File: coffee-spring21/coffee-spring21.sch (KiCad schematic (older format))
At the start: 54 parts, among them J1 AudioPlug3, SW1 SW_SPDT, U1 MAX2750AUA+, U11 SMA_PCB_Edge_Mount, U2 Opamp_Quad_Generic, U5 SMA_PCB_Edge_Mount, U6 SMA_PCB_Edge_Mount, U9 ADE-3G+

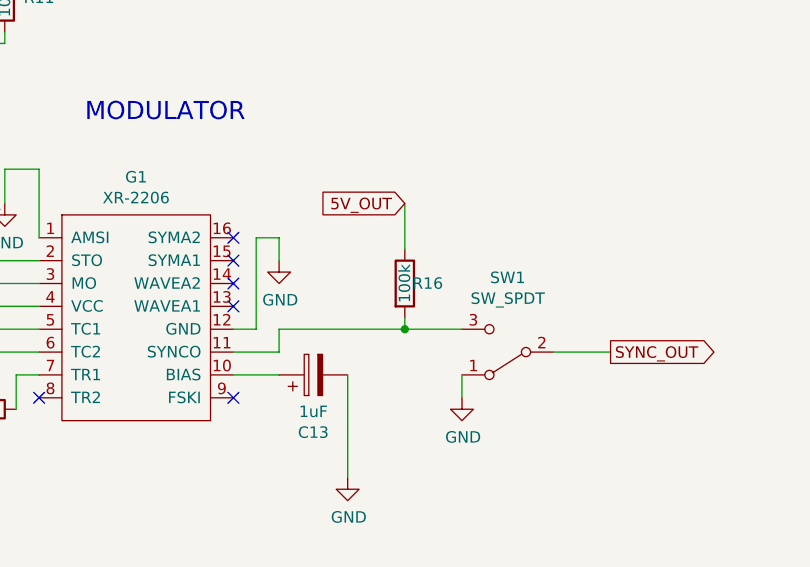
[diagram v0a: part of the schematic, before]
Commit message: Modified CCR layout
Added through hold resistors, power and ground terminals for SMA PA and LNA.
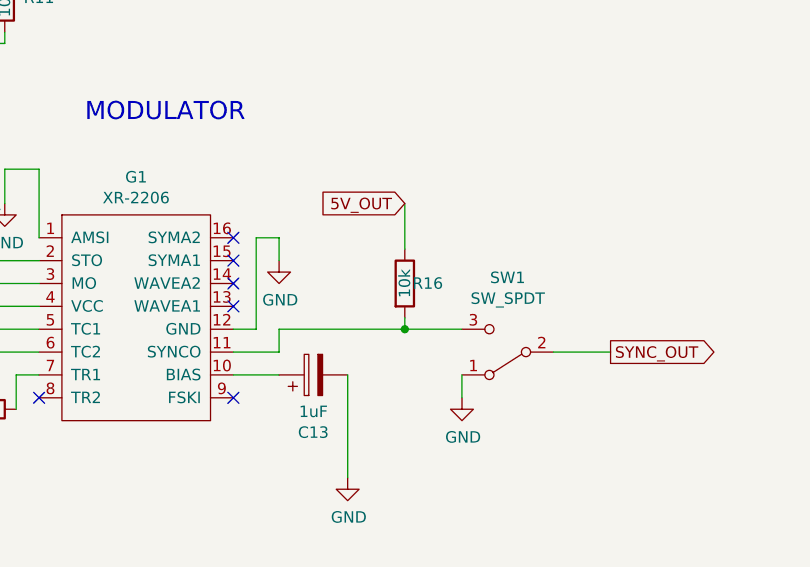
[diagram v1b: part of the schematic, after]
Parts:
- R16: value 100k -> 10k
- R18: footprint Resistor_SMD:R_0805_2012Metric -> Resistor_THT:R_Axial_DIN0207_L6.3mm_D2.5mm_P7.62mm_Horizontal
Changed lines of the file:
@@
 	3550 4750 3550 5000
-Wire Wire Line
-	1350 2850 1350 2900
-$Comp
-L power:GND #PWR0126
-U 1 1 6045E0E7
-P 1350 2900
-F 0 "#PWR0126" H 1350 2650 50  0001 C CNN
-F 1 "GND" H 1355 2727 50  0000 C CNN
-F 2 "" H 1350 2900 50  0001 C CNN
-F 3 "" H 1350 2900 50  0001 C CNN
-	1    1350 2900
-	1    0    0    -1
-$EndComp
-$Comp
-L Device:Battery BT2
-U 1 1 6045E0E6
-P 1350 2650
-F 0 "BT2" H 1550 2700 50  0000 C CNN
-F 1 "6V" H 1550 2600 50  0000 C CNN
-F 2 "Connector_PinSocket_2.54mm:PinSocket_1x02_P2.54mm_Vertical" V 1350 2710 50  0001 C CNN
-F 3 "~" V 1350 2710 50  0001 C CNN
-	1    1350 2650
-	1    0    0    -1
-$EndComp
 Wire Wire Line
 	1350 2050 1350 2300
@@
 	1    0    0    -1
 $EndComp
-Wire Wire Line
-	1350 1250 1350 1650
 Connection ~ 2150 2300
 Wire Wire Line
@@
 	1800 1250 2050 1250
 Connection ~ 1800 1250
-Wire Wire Line
-	1350 1250 1800 1250
 $Comp
 L power:GND #PWR0104
@@
 Wire Wire Line
 	12200 3100 11750 3100
-Wire Wire Line
-	1350 2300 1350 2450
-Connection ~ 1350 2300
 Text GLabel 11750 3100 0    50   Output ~ 0
 IF_SIGNAL
@@
 F 0 "R18" H 8800 6850 50  0000 C CNN
 F 1 "220" V 8700 6850 50  0000 C CNN
-F 2 "Resistor_SMD:R_0805_2012Metric" V 8630 6850 50  0001 C CNN
+F 2 "Resistor_THT:R_Axial_DIN0207_L6.3mm_D2.5mm_P7.62mm_Horizontal" V 8630 6850 50  0001 C CNN
 F 3 "~" H 8700 6850 50  0001 C CNN
 	1    8700 6850
@@
 P 5600 6050
 F 0 "R16" H 5700 6050 50  0000 C CNN
-F 1 "100k" V 5600 6050 50  0000 C CNN
+F 1 "10k" V 5600 6050 50  0000 C CNN
 F 2 "Resistor_SMD:R_0805_2012Metric" V 5530 6050 50  0001 C CNN
 F 3 "~" H 5600 6050 50  0001 C CNN
@@
 	1    0    0    -1
 $EndComp
+Wire Wire Line
+	1350 1250 1800 1250
+Wire Wire Line
+	1350 1250 1350 1650
+Connection ~ 1350 2300
+Wire Wire Line
+	1350 2300 1350 2450
+$Comp
+L Device:Battery BT2
+U 1 1 6045E0E6
+P 1350 2650
+F 0 "BT2" H 1550 2700 50  0000 C CNN
+F 1 "6V" H 1550 2600 50  0000 C CNN
+F 2 "Connector_PinSocket_2.54mm:PinSocket_1x02_P2.54mm_Vertical" V 1350 2710 50  0001 C CNN
+F 3 "~" V 1350 2710 50  0001 C CNN
+	1    1350 2650
+	1    0    0    -1
+$EndComp
+$Comp
+L power:GND #PWR0126
+U 1 1 6045E0E7
+P 1350 2900
+F 0 "#PWR0126" H 1350 2650 50  0001 C CNN
+F 1 "GND" H 1355 2727 50  0000 C CNN
+F 2 "" H 1350 2900 50  0001 C CNN
+F 3 "" H 1350 2900 50  0001 C CNN
+	1    1350 2900
+	1    0    0    -1
+$EndComp
+Wire Wire Line
+	1350 2850 1350 2900
 $EndSCHEMATC

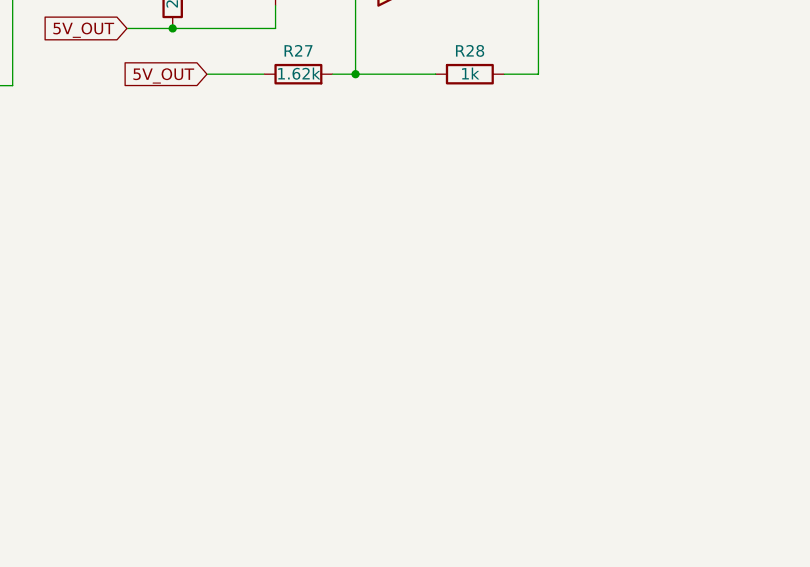
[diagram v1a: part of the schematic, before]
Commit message: Board edits before fabricating
Via stitching, unused op-amp arrangement
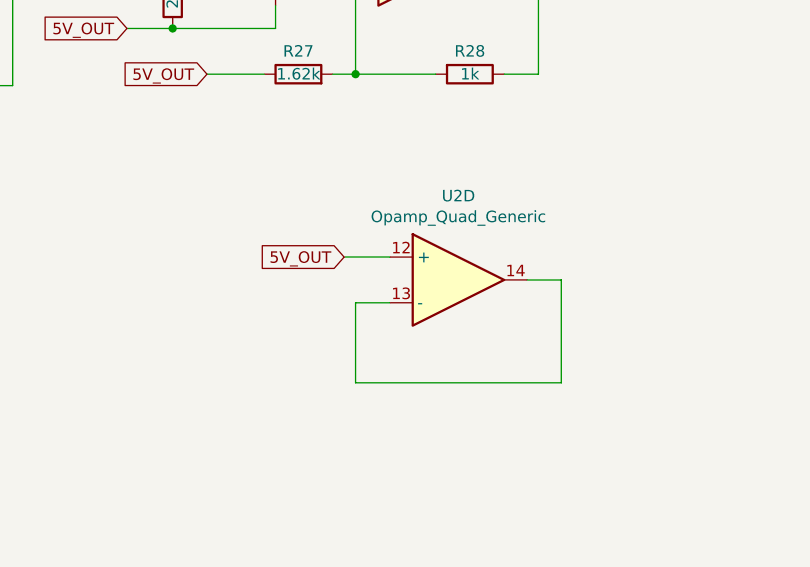
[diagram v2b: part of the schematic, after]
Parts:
- added unit 4 of U2
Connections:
- net 5V_OUT: now also U2.12 (+)
- new net: U2.13 (-), U2.14
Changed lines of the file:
@@
 Sheet 1 1
 Title "Coffee Can Radar"
-Date ""
+Date "2021-04-18"
 Rev "1"
 Comp "Husky Satellite Lab"
-Comment1 "Austin Burnham"
+Comment1 ""
 Comment2 ""
 Comment3 ""
@@
 Wire Wire Line
 	1350 2850 1350 2900
+$Comp
+L Device:Opamp_Quad_Generic U2
+U 4 1 607862C8
+P 13850 7450
+F 0 "U2" H 13850 7817 50  0000 C CNN
+F 1 "Opamp_Quad_Generic" H 13850 7726 50  0000 C CNN
+F 2 "" H 13850 7450 50  0001 C CNN
+F 3 "~" H 13850 7450 50  0001 C CNN
+	4    13850 7450
+	1    0    0    -1
+$EndComp
+Text GLabel 13350 7350 0    50   Input ~ 0
+5V_OUT
+Wire Wire Line
+	13550 7350 13350 7350
+Wire Wire Line
+	14150 7450 14300 7450
+Wire Wire Line
+	14300 7450 14300 7900
+Wire Wire Line
+	14300 7900 13400 7900
+Wire Wire Line
+	13400 7900 13400 7550
+Wire Wire Line
+	13400 7550 13550 7550
 $EndSCHEMATC
